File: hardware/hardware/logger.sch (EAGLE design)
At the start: 29 parts

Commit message: Oops, A16 connected to RB2
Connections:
- net A16: now also MCU.RB2/AN8/INT2/VMO
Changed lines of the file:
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@@
 <?xml version="1.0" encoding="utf-8"?>
 <!DOCTYPE eagle SYSTEM "eagle.dtd">
-<eagle version="6.1">
+<eagle version="6.2">
 <drawing>
 <settings>
@@
 <label x="223.52" y="160.02" size="1.27" layer="95" rot="R180" xref="yes"/>
 </segment>
-</net>
+<segment>
+<pinref part="MCU" gate="G$1" pin="RB2/AN8/INT2/VMO"/>
+<wire x1="279.4" y1="215.9" x2="281.94" y2="215.9" width="0.1524" layer="91"/>
+<label x="281.94" y="215.9" size="1.27" layer="95" xref="yes"/>
+</segment>
+</net>

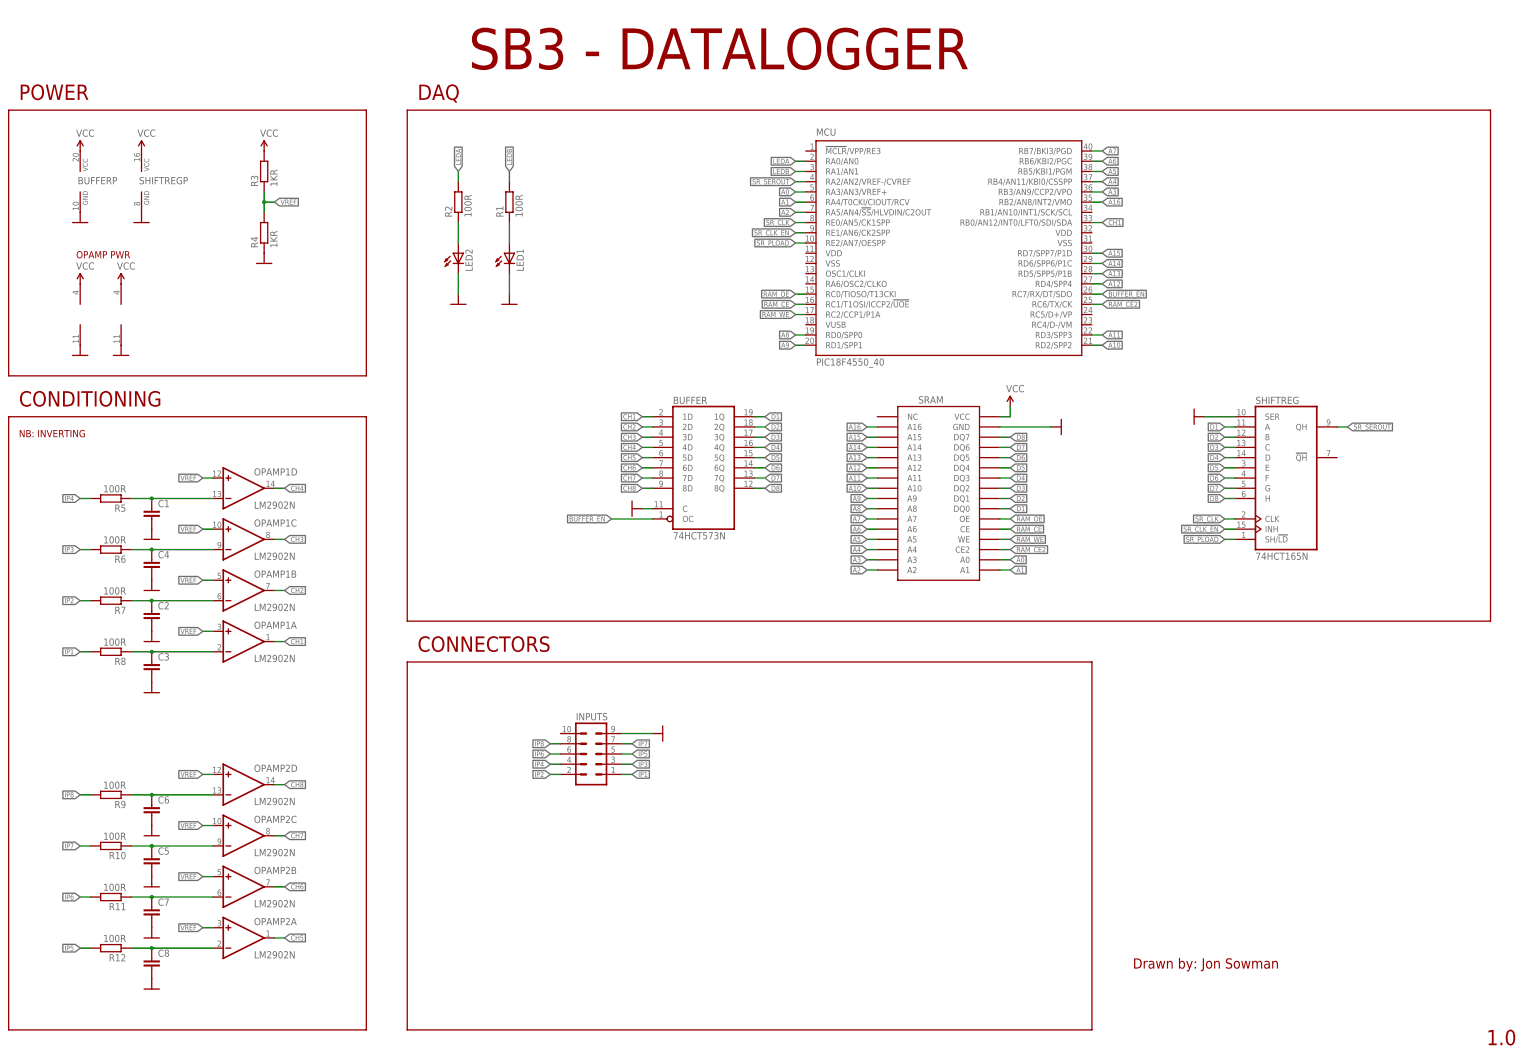
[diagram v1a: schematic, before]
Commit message: Fixed all issues in schematic. Closes #11
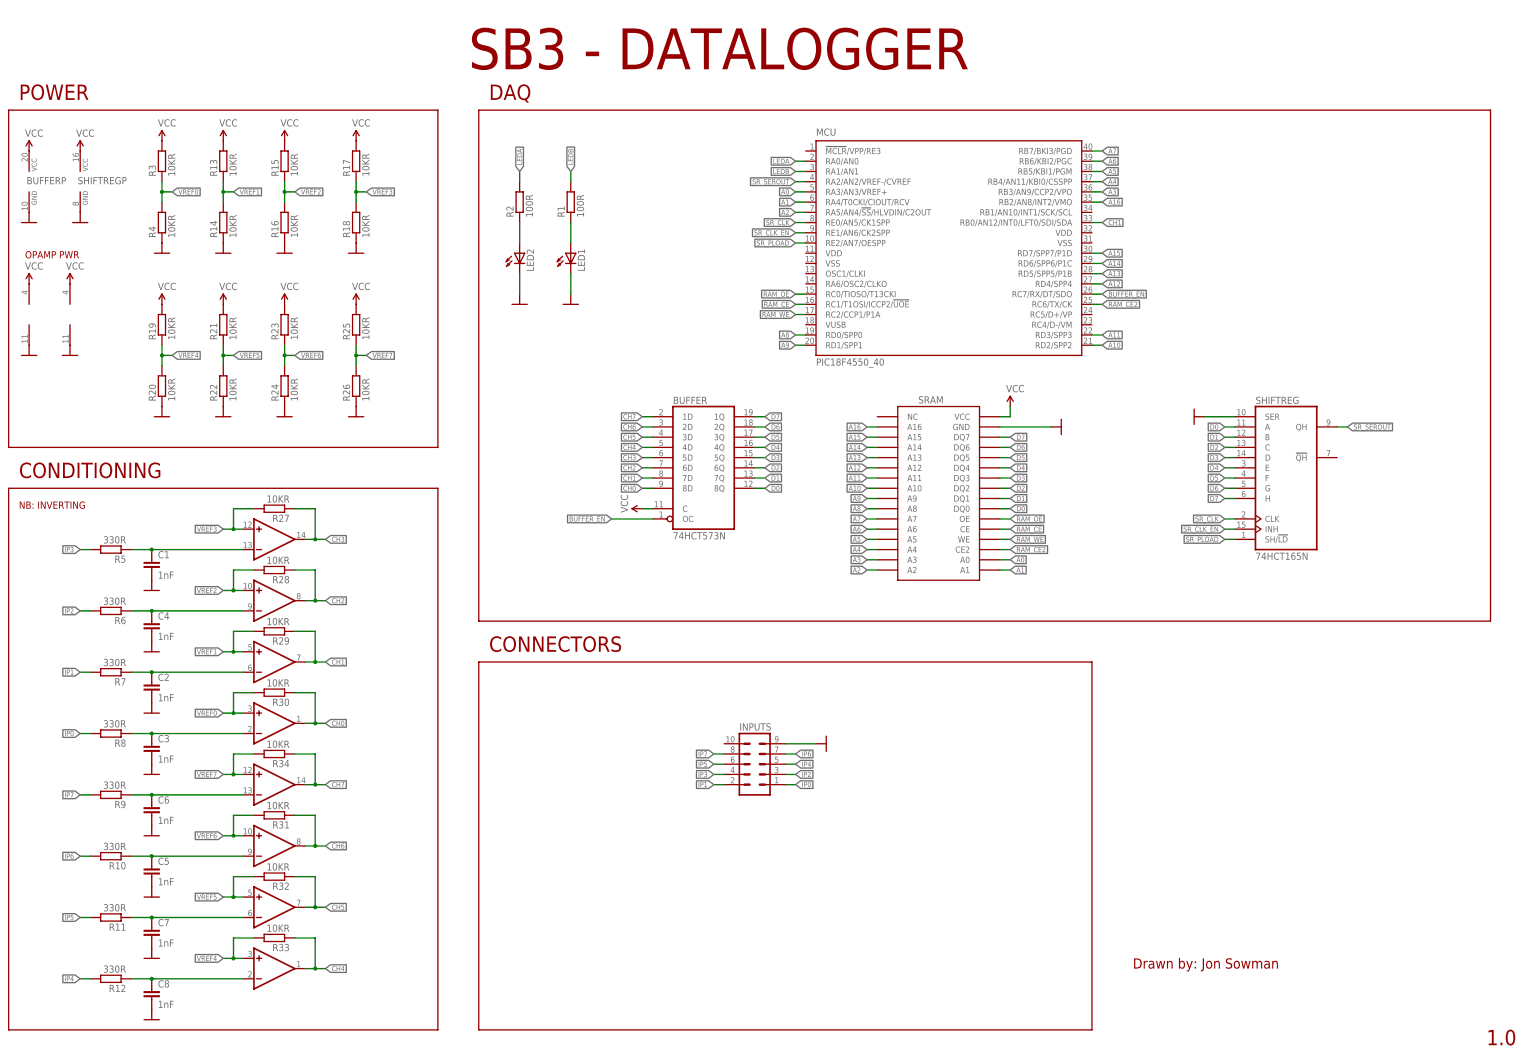
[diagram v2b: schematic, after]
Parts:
- added R13, R14, R15, R16, R17, R18, R19, R20, R21, R22, R23, R24, R25, R26, R27, R28, R29, R30, R31, R32, R33, R34: 10KR, rcl:R-EU_0207/10
- C1, C2, C3, C4, C5, C6, C7, C8: value (none) -> 1nF
- R10, R11, R12, R5, R6, R7, R8, R9: value 100R -> 330R
- R3, R4: value 1KR -> 10KR
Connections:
- removed net CH8: BUFFERA.8D, OPAMP2D.OUT
- removed net D8: BUFFERA.8Q, SHIFTREGA.H, SRAM.DQ7
- removed net IP8: INPUTS.8, R9.2
- removed net VREF: OPAMP1A.+IN, OPAMP1B.+IN, OPAMP1C.+IN, OPAMP1D.+IN, OPAMP2A.+IN, OPAMP2B.+IN, OPAMP2C.+IN, OPAMP2D.+IN, R3.1, R4.2
- new net CH0: BUFFERA.8D, OPAMP1A.OUT, R30.1
- new net D0: BUFFERA.8Q, SHIFTREGA.A, SRAM.DQ0
- new net IP0: INPUTS.1, R8.2
- new net VREF0: OPAMP1A.+IN, R3.1, R30.2, R4.2
- new net VREF1: OPAMP1B.+IN, R13.1, R14.2, R29.2
- new net VREF2: OPAMP1C.+IN, R15.1, R16.2, R28.2
- new net VREF3: OPAMP1D.+IN, R17.1, R18.2, R27.2
- new net VREF4: OPAMP2A.+IN, R19.1, R20.2, R33.2
- new net VREF5: OPAMP2B.+IN, R21.1, R22.2, R32.2
- new net VREF6: OPAMP2C.+IN, R23.1, R24.2, R31.2
- new net VREF7: OPAMP2D.+IN, R25.1, R26.2, R34.2
- net CH1: now also BUFFERA.7D, OPAMP1B.OUT, R29.1; no longer BUFFERA.1D, OPAMP1A.OUT
- net CH2: now also BUFFERA.6D, OPAMP1C.OUT, R28.1; no longer BUFFERA.2D, OPAMP1B.OUT
- net CH3: now also BUFFERA.5D, OPAMP1D.OUT, R27.1; no longer BUFFERA.3D, OPAMP1C.OUT
- net CH4: now also OPAMP2A.OUT, R33.1; no longer OPAMP1D.OUT
- net CH5: now also BUFFERA.3D, OPAMP2B.OUT, R32.1; no longer BUFFERA.5D, OPAMP2A.OUT
- net CH6: now also BUFFERA.2D, OPAMP2C.OUT, R31.1; no longer BUFFERA.6D, OPAMP2B.OUT
- net CH7: now also BUFFERA.1D, OPAMP2D.OUT, R34.1; no longer BUFFERA.7D, OPAMP2C.OUT
- net D1: now also BUFFERA.7Q, SHIFTREGA.B, SRAM.DQ1; no longer BUFFERA.1Q, SHIFTREGA.A, SRAM.DQ0
- net D2: now also BUFFERA.6Q, SHIFTREGA.C, SRAM.DQ2; no longer BUFFERA.2Q, SHIFTREGA.B, SRAM.DQ1
- net D3: now also BUFFERA.5Q, SHIFTREGA.D, SRAM.DQ3; no longer BUFFERA.3Q, SHIFTREGA.C, SRAM.DQ2
- net D4: now also SHIFTREGA.E, SRAM.DQ4; no longer SHIFTREGA.D, SRAM.DQ3
- net D5: now also BUFFERA.3Q, SHIFTREGA.F, SRAM.DQ5; no longer BUFFERA.5Q, SHIFTREGA.E, SRAM.DQ4
- net D6: now also BUFFERA.2Q, SHIFTREGA.G, SRAM.DQ6; no longer BUFFERA.6Q, SHIFTREGA.F, SRAM.DQ5
- net D7: now also BUFFERA.1Q, SHIFTREGA.H, SRAM.DQ7; no longer BUFFERA.7Q, SHIFTREGA.G, SRAM.DQ6
- net GND: now also R14.1, R16.1, R18.1, R20.1, R22.1, R24.1, R26.1; no longer BUFFERA.C
- net IP1: now also INPUTS.2, R7.2; no longer INPUTS.1, R8.2
- net IP2: now also INPUTS.3, R6.2; no longer INPUTS.2, R7.2
- net IP3: now also INPUTS.4, R5.2; no longer INPUTS.3, R6.2
- net IP4: now also INPUTS.5, R12.2; no longer INPUTS.4, R5.2
- net IP5: now also INPUTS.6, R11.2; no longer INPUTS.5, R12.2
- net IP6: now also INPUTS.7, R10.2; no longer INPUTS.6, R11.2
- net IP7: now also INPUTS.8, R9.2; no longer INPUTS.7, R10.2
- net VCC: now also BUFFERA.C, R13.2, R15.2, R17.2, R19.2, R21.2, R23.2, R25.2
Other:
- moved on the sheet: BUFFERP, C1, C2, C3, C4, C5, C7, C8, INPUTS, LED1, LED2, R1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

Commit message: Updated resistor values for LEDs
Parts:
- R1: value 100R -> 120R
- R2: value 100R -> 56R
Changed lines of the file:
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@@
 <part name="GND5" library="SparkFun" deviceset="GND" device=""/>
 <part name="MCU" library="microchip" deviceset="PIC18F4*_40" device="" technology="550"/>
-<part name="R1" library="rcl" deviceset="R-EU_" device="0207/10" value="100R"/>
+<part name="R1" library="rcl" deviceset="R-EU_" device="0207/10" value="120R"/>
 <part name="LED1" library="led" deviceset="LED" device="5MM"/>
 <part name="GND6" library="SparkFun" deviceset="GND" device=""/>
-<part name="R2" library="rcl" deviceset="R-EU_" device="0207/10" value="100R"/>
+<part name="R2" library="rcl" deviceset="R-EU_" device="0207/10" value="56R"/>
 <part name="LED2" library="led" deviceset="LED" device="5MM"/>
 <part name="GND7" library="SparkFun" deviceset="GND" device=""/>

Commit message: Testing LEDs, swapped round on schematic to match hardware changes
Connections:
- net LEDA: now also R1.2; no longer R2.2
- net LEDB: now also R2.2; no longer R1.2
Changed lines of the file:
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@@
 </segment>
 <segment>
-<pinref part="R2" gate="G$1" pin="2"/>
-<wire x1="137.16" y1="223.52" x2="137.16" y2="220.98" width="0.1524" layer="91"/>
-<label x="137.16" y="223.52" size="1.27" layer="95" rot="R90" xref="yes"/>
+<pinref part="R1" gate="G$1" pin="2"/>
+<wire x1="149.86" y1="223.52" x2="149.86" y2="220.98" width="0.1524" layer="91"/>
+<label x="149.86" y="223.52" size="1.27" layer="95" rot="R90" xref="yes"/>
 </segment>
 </net>
@@
 </segment>
 <segment>
-<pinref part="R1" gate="G$1" pin="2"/>
-<wire x1="149.86" y1="223.52" x2="149.86" y2="220.98" width="0.1524" layer="91"/>
-<label x="149.86" y="223.52" size="1.27" layer="95" rot="R90" xref="yes"/>
+<pinref part="R2" gate="G$1" pin="2"/>
+<wire x1="137.16" y1="223.52" x2="137.16" y2="220.98" width="0.1524" layer="91"/>
+<label x="137.16" y="223.52" size="1.27" layer="95" rot="R90" xref="yes"/>
 </segment>
 </net>

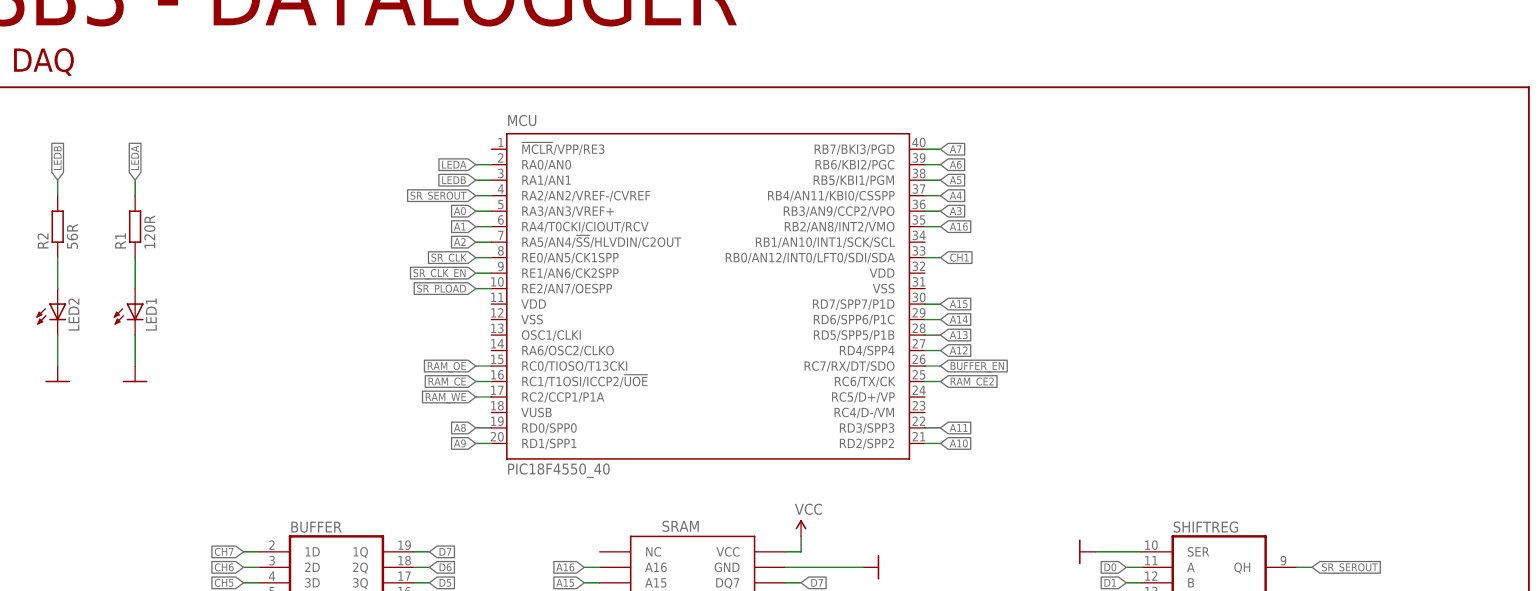
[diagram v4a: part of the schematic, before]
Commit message: Pushed schematic with hw addressing and a new PNG render
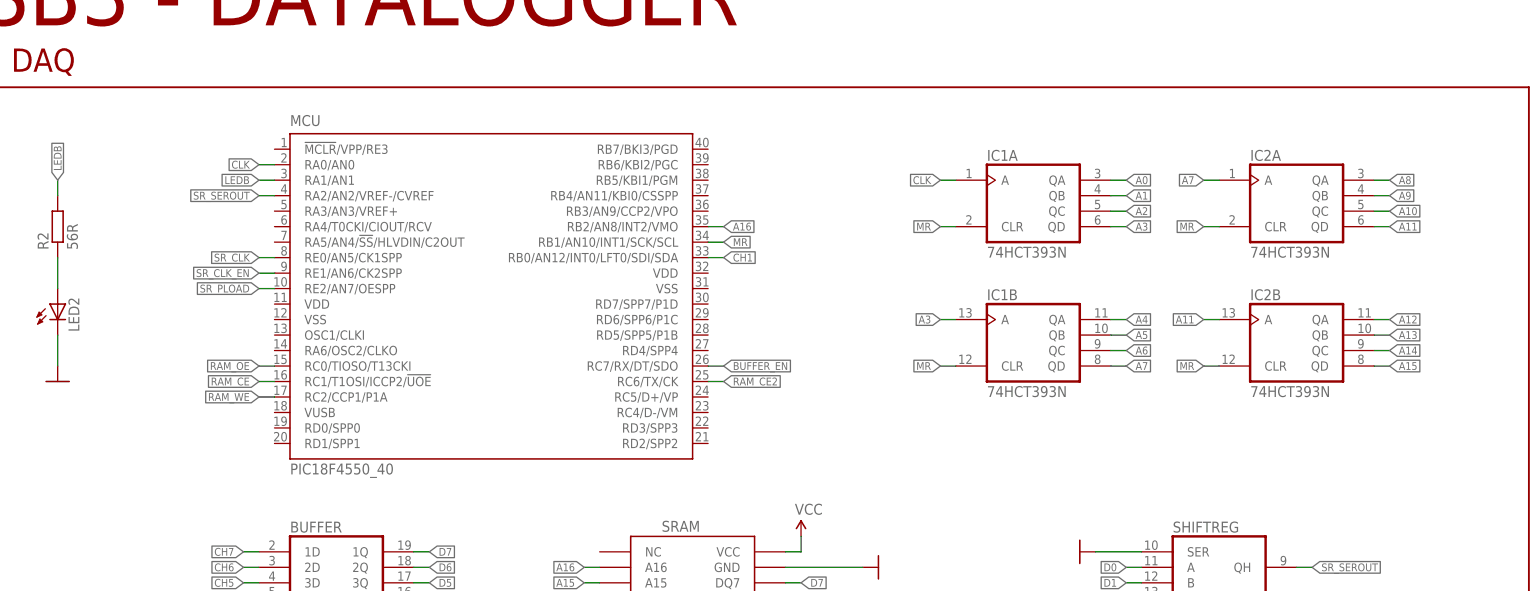
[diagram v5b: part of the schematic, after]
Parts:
- removed LED1: (no value), led:LED5MM
- removed R1: 120R, rcl:R-EU_0207/10
- added IC1, IC2: 74HCT393N, 74xx-eu:74HCT393N
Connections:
- removed net LEDA: MCU.RA0/AN0, R1.2
- removed net N$2: LED1.A, R1.1
- new net CLK: IC1A.A, MCU.RA0/AN0
- new net MR: IC1A.CLR, IC1B.CLR, IC2A.CLR, IC2B.CLR, MCU.RB1/AN10/INT1/SCK/SCL
- net A0: now also IC1A.QA; no longer MCU.RA3/AN3/VREF+
- net A1: now also IC1A.QB; no longer MCU.RA4/T0CKI/CIOUT/RCV
- net A10: now also IC2A.QC; no longer MCU.RD2/SPP2
- net A11: now also IC2A.QD, IC2B.A; no longer MCU.RD3/SPP3
- net A12: now also IC2B.QA; no longer MCU.RD4/SPP4
- net A13: now also IC2B.QB; no longer MCU.RD5/SPP5/P1B
- net A14: now also IC2B.QC; no longer MCU.RD6/SPP6/P1C
- net A15: now also IC2B.QD; no longer MCU.RD7/SPP7/P1D
- net A2: now also IC1A.QC; no longer MCU.RA5/AN4/!SS!/HLVDIN/C2OUT
- net A3: now also IC1A.QD, IC1B.A; no longer MCU.RB3/AN9/CCP2/VPO
- net A4: now also IC1B.QA; no longer MCU.RB4/AN11/KBI0/CSSPP
- net A5: now also IC1B.QB; no longer MCU.RB5/KBI1/PGM
- net A6: now also IC1B.QC; no longer MCU.RB6/KBI2/PGC
- net A7: now also IC1B.QD, IC2A.A; no longer MCU.RB7/BKI3/PGD
- net A8: now also IC2A.QA; no longer MCU.RD0/SPP0
- net A9: now also IC2A.QB; no longer MCU.RD1/SPP1
- net GND: no longer LED1.C
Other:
- moved on the sheet: MCU
